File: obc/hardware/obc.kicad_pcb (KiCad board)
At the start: 4 copper layers, 80 x 80 mm, 61 parts, among them J1 Conn_ARM_JTAG_SWD_10, J2 Micro_SD_Card, J3 Conn_Coaxial, J4 USB_C_Receptacle_USB2.0_16P, J5 Conn_Coaxial, SW1 SW_SPDT, SW2 SW_Push, U1 STM32H743ZGT6, U2 RFM96W-433S2, U3 MAX6369, U4 MAX-M10S, U5 FM24CL16B, U6 MS5607-02BA, Y1 25 MHz, Y2 32.768 kHz

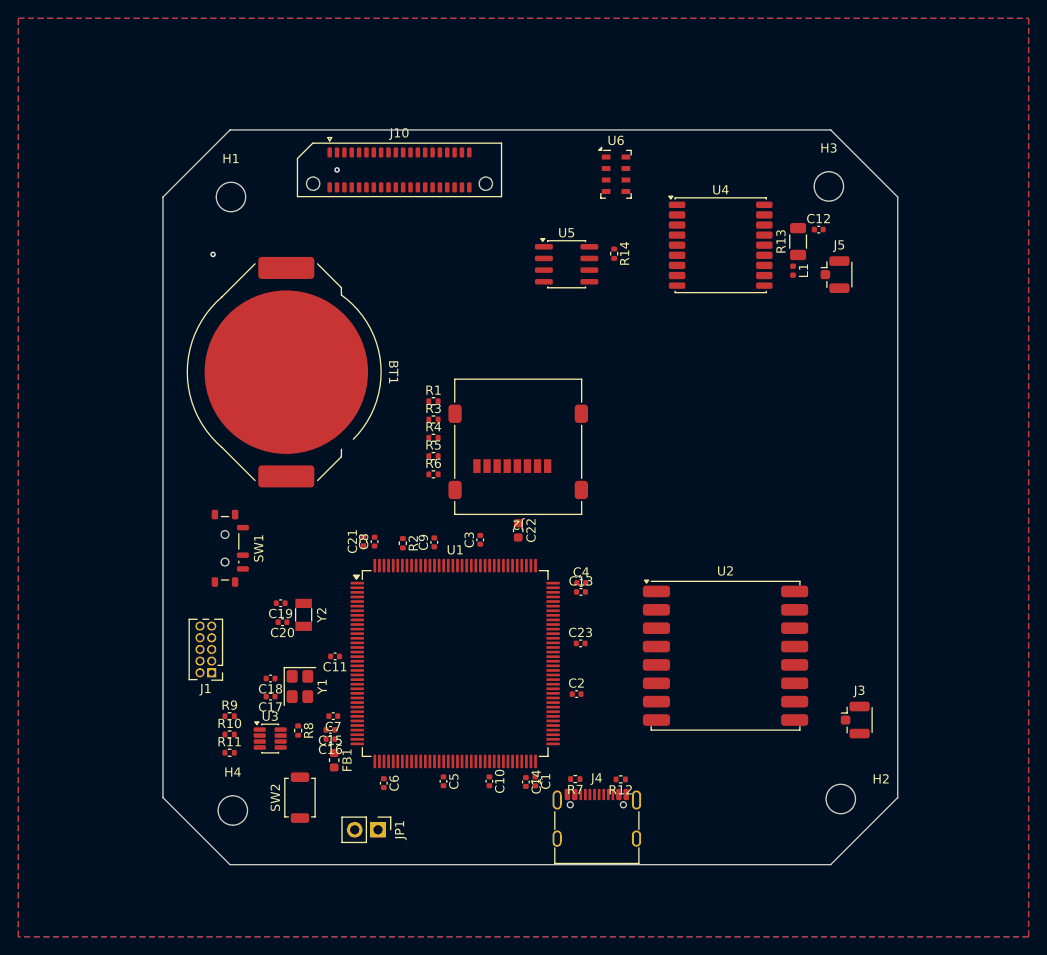
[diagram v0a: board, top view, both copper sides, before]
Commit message: added CAN, UART, supervisor, USB, power OR-ing, GPS, did layout
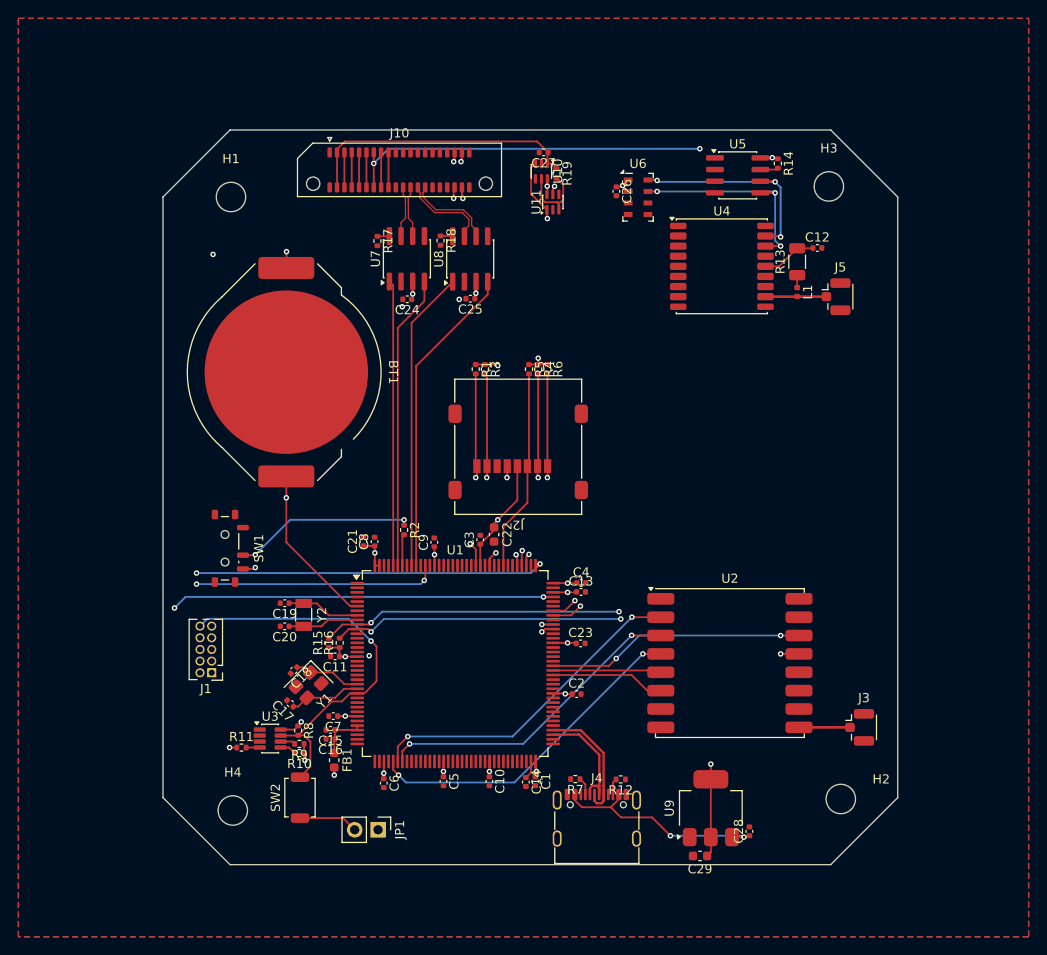
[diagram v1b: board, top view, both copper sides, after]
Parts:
- added C24: 100nF, Capacitor_SMD:C_0402_1005Metric, F.Cu at (117.3, 70.6)
- added C25: 100nF, Capacitor_SMD:C_0402_1005Metric, F.Cu at (124.2, 70.5)
- added C26: 100nF, Capacitor_SMD:C_0402_1005Metric, F.Cu at (140.1, 58.8)
- added C27: 10u, Capacitor_SMD:C_0402_1005Metric, F.Cu at (132.2, 54.6)
- added C28: 10u, Capacitor_SMD:C_0402_1005Metric, F.Cu at (154.6, 128.5)
- added C29: 22u, Capacitor_SMD:C_0603_1608Metric, F.Cu at (149.2, 131.2)
- added R15: 10k, Resistor_SMD:R_0402_1005Metric, F.Cu at (108.8, 108.0)
- added R16: 10k, Resistor_SMD:R_0402_1005Metric, F.Cu at (110.0, 108.0)
- added R17: 51k, Resistor_SMD:R_0402_1005Metric, F.Cu at (114.1, 64.2)
- added R18: 51k, Resistor_SMD:R_0402_1005Metric, F.Cu at (121.0, 64.2)
- added R19: 10k, Resistor_SMD:R_0402_1005Metric, F.Cu at (133.6, 56.9)
- added U10: LM66100DCK, Package_TO_SOT_SMD:SOT-363_SC-70-6, F.Cu at (131.9, 56.6)
- added U11: LM66100DCK, Package_TO_SOT_SMD:SOT-363_SC-70-6, F.Cu at (133.2, 60.0)
- added U7: SN65HVD230, Package_SO:SOIC-8_3.9x4.9mm_P1.27mm, F.Cu at (117.3, 66.2)
- added U8: SN65HVD230, Package_SO:SOIC-8_3.9x4.9mm_P1.27mm, F.Cu at (124.2, 66.2)
- added U9: AMS1117-3.3, Package_TO_SOT_SMD:SOT-223-3_TabPin2, F.Cu at (150.4, 126.0)
- moved U5 21.0 mm to (153.3, 57.1)
- moved R14 20.4 mm to (157.7, 55.8)
- moved R6 16.9 mm to (132.6, 78.2), turned to -90 degrees
- moved R5 14.1 mm to (130.6, 78.2), turned to -90 degrees
- moved R4 13.6 mm to (131.6, 78.2), turned to -90 degrees
- moved R9 8.17 mm to (105.6, 119.0), turned to 180 degrees
- moved R10 7.86 mm to (105.6, 120.0), turned to 180 degrees
- moved R3 7.84 mm to (125.8, 78.2), turned to -90 degrees
- moved R1 5.77 mm to (124.8, 78.2), turned to -90 degrees
- moved U6 3.47 mm to (142.5, 59.5)
- moved C18 2.69 mm to (105.0, 111.0), turned to -135 degrees
- moved C22 2.66 mm to (126.8, 96.2)
- moved J5 2.40 mm to (164.5, 70.3)
- moved L1 2.37 mm to (159.8, 69.8)
- moved U4 2.30 mm to (151.6, 67.0)
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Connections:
- net Net-(J5-In) renamed /STM32H7/Sensors/GPS_ANT
- C1 pad 1: +3.3V -> +3V3
- C10 pad 1: +3.3V -> +3V3
- C11 pad 1: +3.3V -> +3V3
- C2 pad 1: +3.3V -> +3V3
- C21 pad 1: +3.3V -> +3V3
- C22 pad 1: +3.3V -> +3V3
- C23 pad 1: +3.3V -> +3V3
- C3 pad 1: +3.3V -> +3V3
- C4 pad 1: +3.3V -> +3V3
- C5 pad 1: +3.3V -> +3V3
- C6 pad 1: +3.3V -> +3V3
- C7 pad 1: +3.3V -> +3V3
- C8 pad 1: +3.3V -> +3V3
- C9 pad 1: +3.3V -> +3V3
- FB1 pad 2: +3.3V -> +3V3
- J1 pad 1: +3.3V -> +3V3
- J10 pad 13: /Inter-Board-Connector/RAIL_6_VOUT -> VDD_RADIO
- J10 pad 14: /Inter-Board-Connector/RAIL_6_VOUT -> VDD_RADIO
- J10 pad 22: unconnected-(J10-Pin_22-Pad22) -> /Inter-Board-Connector/CAN_MAIN+
- J10 pad 24: unconnected-(J10-Pin_24-Pad24) -> /Inter-Board-Connector/CAN_MAIN-
- J10 pad 26: unconnected-(J10-Pin_26-Pad26) -> /Inter-Board-Connector/CAN_AUX+
- J10 pad 28: unconnected-(J10-Pin_28-Pad28) -> /Inter-Board-Connector/CAN_AUX-
- J10 pad 3: +3.3V -> /Inter-Board-Connector/RAIL_1_VOUT
- J10 pad 4: +3.3V -> /Inter-Board-Connector/RAIL_1_VOUT
- J2 pad 4: +3.3V -> +3V3
- R1 pad 1: +3.3V -> +3V3
- R10 pad 1: +3.3V -> +3V3
- R11 pad 1: +3.3V -> +3V3
- R14 pad 1: +3.3V -> +3V3
- R3 pad 1: +3.3V -> +3V3
- R4 pad 1: +3.3V -> +3V3
- R5 pad 1: +3.3V -> +3V3
- R6 pad 1: +3.3V -> +3V3
- R8 pad 1: +3.3V -> +3V3
- R9 pad 1: +3.3V -> +3V3
- SW1 pad 3: +3.3V -> +3V3
- U1 pad 10: unconnected-(U1-PF0-Pad10) -> SDA
- U1 pad 101: unconnected-(U1-PA9-Pad101) -> /Inter-Board-Connector/SYSTEM_MAIN_UART_TX
- U1 pad 102: unconnected-(U1-PA10-Pad102) -> /Inter-Board-Connector/SYSTEM_MAIN_UART_RX
- U1 pad 108: +3.3V -> +3V3
- U1 pad 11: unconnected-(U1-PF1-Pad11) -> SCL
- U1 pad 119: unconnected-(U1-PD5-Pad119) -> /Inter-Board-Connector/SYSTEM_AUX_UART_TX
- U1 pad 121: +3.3V -> +3V3
- U1 pad 122: unconnected-(U1-PD6-Pad122) -> /Inter-Board-Connector/SYSTEM_AUX_UART_RX
- U1 pad 131: +3.3V -> +3V3
- U1 pad 135: unconnected-(U1-PB5-Pad135) -> /STM32H7/CAN2_RX
- U1 pad 136: unconnected-(U1-PB6-Pad136) -> /STM32H7/CAN2_TX
- U1 pad 139: unconnected-(U1-PB8-Pad139) -> /STM32H7/CAN1_RX
- U1 pad 140: unconnected-(U1-PB9-Pad140) -> /STM32H7/CAN1_TX
- U1 pad 143: +3.3V -> +3V3
- U1 pad 144: +3.3V -> +3V3
- U1 pad 17: +3.3V -> +3V3
- U1 pad 30: +3.3V -> +3V3
- U1 pad 39: +3.3V -> +3V3
- U1 pad 41: unconnected-(U1-PA5-Pad41) -> /STM32H7/SPI1_SCK
- U1 pad 42: unconnected-(U1-PA6-Pad42) -> /STM32H7/SPI1_MISO
- U1 pad 43: unconnected-(U1-PA7-Pad43) -> /STM32H7/SPI1_MOSI
- U1 pad 52: +3.3V -> +3V3
- U1 pad 62: +3.3V -> +3V3
- U1 pad 72: +3.3V -> +3V3
- U1 pad 75: /STM32H7/USB_D- -> unconnected-(U1-PB14-Pad75)
- U1 pad 76: /STM32H7/USB_D+ -> unconnected-(U1-PB15-Pad76)
- U1 pad 84: +3.3V -> +3V3
- U1 pad 88: unconnected-(U1-PG3-Pad88) -> /STM32H7/~{RADIO_RESET}
- U1 pad 89: unconnected-(U1-PG4-Pad89) -> /STM32H7/~{RADIO_CS}
- U1 pad 90: unconnected-(U1-PG5-Pad90) -> /STM32H7/RADIO_DIO0
- U1 pad 95: +3.3V -> +3V3
- U2 pad 13: +3.3V -> VDD_RADIO
- U2 pad 14: unconnected-(U2-DIO0-Pad14) -> /STM32H7/RADIO_DIO0
- U2 pad 2: /STM32H7/Radio/MISO -> /STM32H7/SPI1_MISO
- U2 pad 3: /STM32H7/Radio/MOSI -> /STM32H7/SPI1_MOSI
- U2 pad 4: /STM32H7/Radio/SCK -> /STM32H7/SPI1_SCK
- U2 pad 5: /STM32H7/Radio/~{CS} -> /STM32H7/~{RADIO_CS}
- U2 pad 6: /STM32H7/Radio/~{RESET} -> /STM32H7/~{RADIO_RESET}
- U3 pad 8: +3.3V -> +3V3
- U5 pad 8: +3.3V -> +3V3
- U6 pad 1: unconnected-(U6-VDD-Pad1) -> +3V3
- U6 pad 2: unconnected-(U6-PS-Pad2) -> +3V3
- U6 pad 3: unconnected-(U6-GND-Pad3) -> GND
- U6 pad 4: Net-(U6-CSB-Pad4) -> GND
- U6 pad 5: Net-(U6-CSB-Pad4) -> GND
- U6 pad 7: unconnected-(U6-SDI/SDA-Pad7) -> SDA
- U6 pad 8: unconnected-(U6-SCLK-Pad8) -> SCL
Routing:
- net SCL: track 0.00 -> 105.1 mm, vias 0 -> 5
- net SDA: track 0.00 -> 103.5 mm, vias 0 -> 5
- net VDD_RADIO: track 0.00 -> 100.6 mm, vias 0 -> 3
- net Net-(U10-~{CE}): track 0.00 -> 83.9 mm, vias 0 -> 2
- net +3V3: track 0.00 -> 62.2 mm, vias 0 -> 24
- net /Inter-Board-Connector/SYSTEM_MAIN_UART_TX: track 0.00 -> 58.2 mm, vias 0 -> 2
- net /Inter-Board-Connector/SYSTEM_MAIN_UART_RX: track 0.00 -> 57.1 mm, vias 0 -> 2
- net /STM32H7/SWDIO: track 0.00 -> 49.9 mm, vias 0 -> 2
- net /STM32H7/SWCLK: track 0.00 -> 49.3 mm, vias 0 -> 2
- net Net-(BT1-+): track 0.00 -> 46.6 mm, vias 0 -> 2
- net /Inter-Board-Connector/SYSTEM_AUX_UART_RX: track 0.00 -> 43.9 mm, vias 0 -> 2
- net /STM32H7/NRST: track 0.00 -> 43.4 mm, vias 0 -> 1
- net /Inter-Board-Connector/SYSTEM_AUX_UART_TX: track 0.00 -> 43.0 mm, vias 0 -> 2
- net /STM32H7/SPI1_SCK: track 0.00 -> 36.4 mm, vias 0 -> 2
- net /STM32H7/SPI1_MISO: track 0.00 -> 36.1 mm, vias 0 -> 2
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- added copper zone on In2.Cu, net +3V3
- removed copper zone on In2.Cu, net +3.3V

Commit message: Redid silkscreen
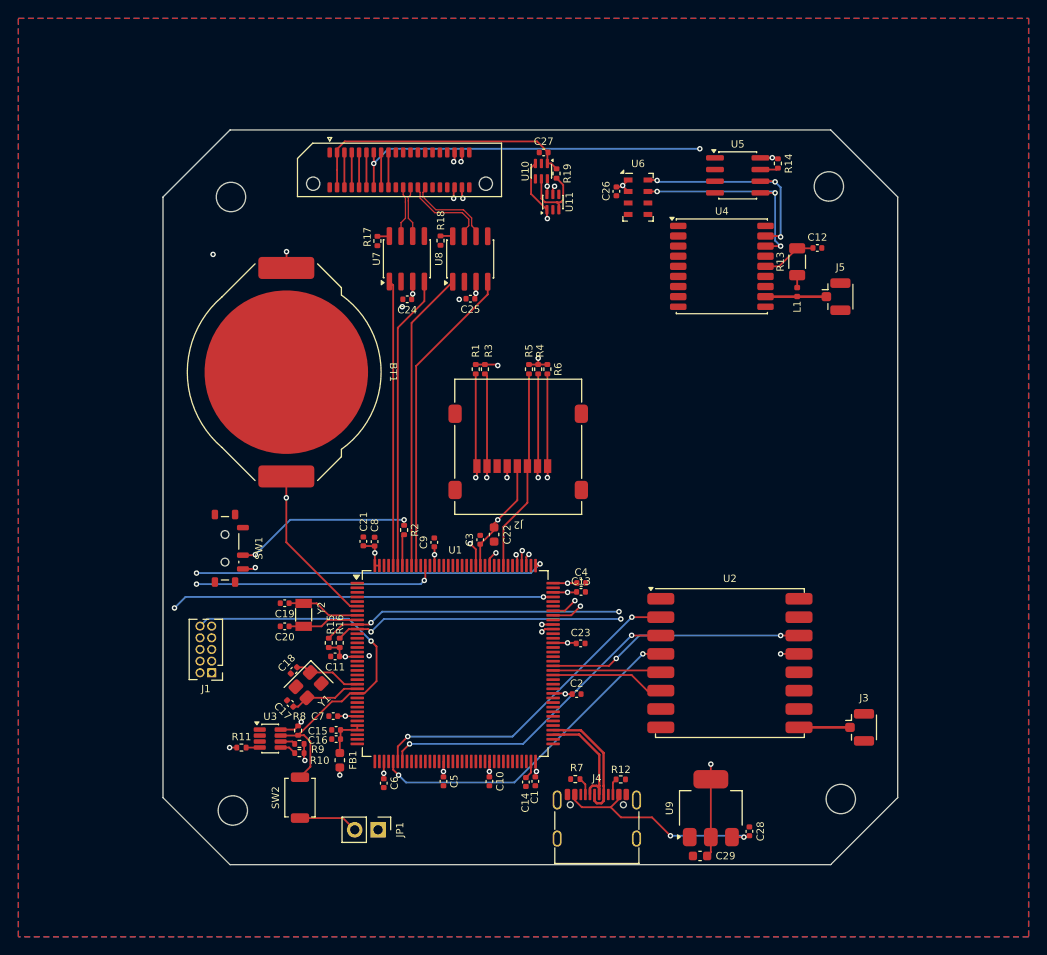
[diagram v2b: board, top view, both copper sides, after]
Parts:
- added REF**: Smolhaj_Scale_0.1, Symbol:Smolhaj_Scale_0.1, B.Cu at (100.6, 69.2)
- added REF**: Smolhaj_Scale_0.1, Symbol:Smolhaj_Scale_0.1, B.Cu at (101.4, 92.2)
- added REF**: Smolhaj_Scale_0.1, Symbol:Smolhaj_Scale_0.1, B.Cu at (101.8, 115.2)
- moved C15 0.61 mm to (109.6, 117.5)
- moved C16 0.61 mm to (109.6, 118.5)
- moved FB1 0.61 mm to (110.0, 120.8)
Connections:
- U1 pad 75: unconnected-(U1-PB14-Pad75) -> /STM32H7/USB_D-
- U1 pad 76: unconnected-(U1-PB15-Pad76) -> /STM32H7/USB_D+
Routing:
- net VDDA: track 5.49 -> 4.88 mm

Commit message: add SCRT and OSU AIAA logos, add IMU, add PPS LED, hook up some IOs
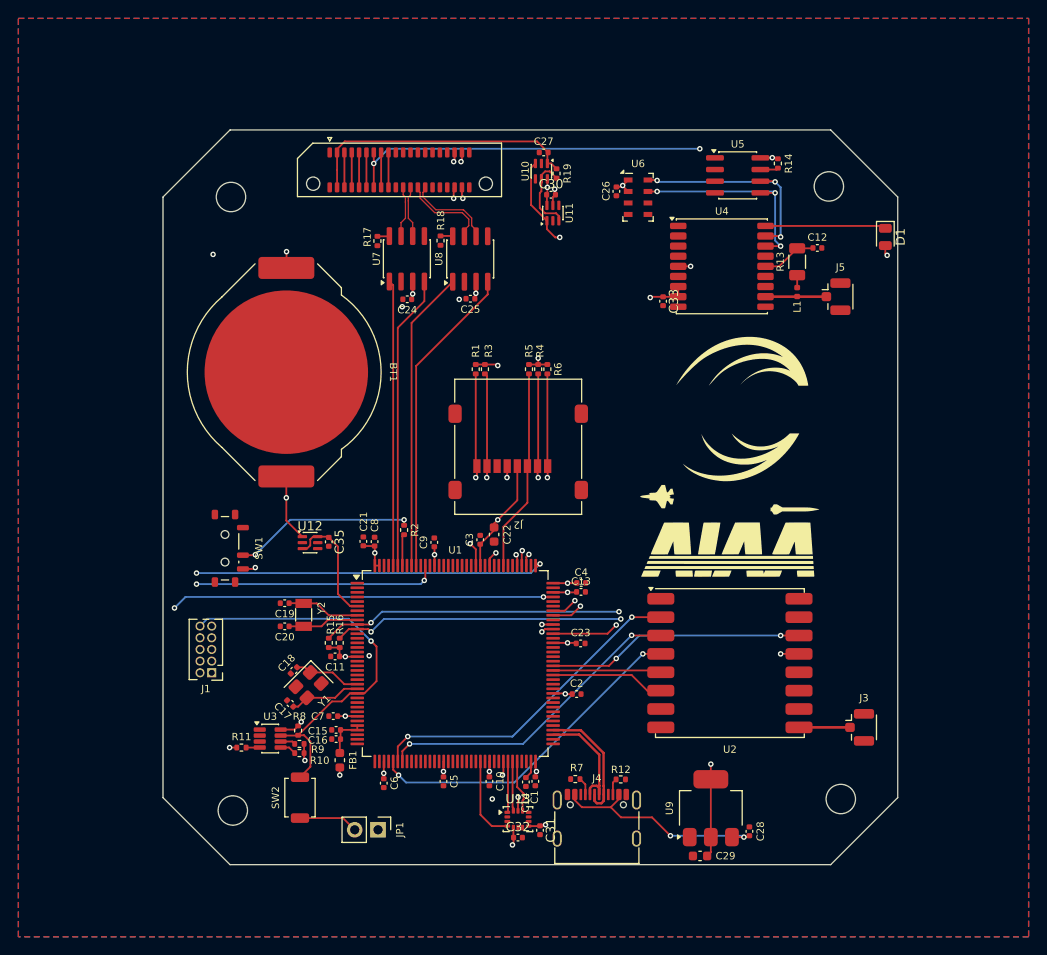
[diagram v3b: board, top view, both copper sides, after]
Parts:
- removed the REF** at (100.6, 69.2)
- removed the REF** at (101.8, 115.2)
- added C30: 10u, Capacitor_SMD:C_0402_1005Metric, F.Cu at (133.0, 59.2)
- added C31: 100nF, Capacitor_SMD:C_0402_1005Metric, F.Cu at (131.8, 128.4)
- added C32: 100nF, Capacitor_SMD:C_0402_1005Metric, F.Cu at (129.4, 129.2)
- added C33: 100nF, Capacitor_SMD:C_0402_1005Metric, F.Cu at (145.2, 70.8)
- added C35: 100nF, Capacitor_SMD:C_0402_1005Metric, F.Cu at (108.8, 97.0)
- added D1: LED, LED_SMD:LED_0805_2012Metric, F.Cu at (169.4, 63.8)
- added REF**: osu-aiaa-logo, obc-footprints:osu-aiaa-logo, F.Cu at (142.8, 100.8)
- added REF**: scrt-logo, obc-footprints:scrt-logo, F.Cu at (153.6, 82.6)
- added U12: LM66100DCK, Package_TO_SOT_SMD:SOT-363_SC-70-6, F.Cu at (106.8, 97.1)
- added U13: LSM6DSM, Package_LGA:LGA-14_3x2.5mm_P0.5mm_LayoutBorder3x4y, F.Cu at (129.4, 127.2)
- moved U11 1.20 mm to (133.2, 61.2)
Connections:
- U1 pad 6: Net-(BT1-+) -> Net-(U1-VBAT)
- U1 pad 60: unconnected-(U1-PE9-Pad60) -> /STM32H7/Sensors/IMU_INTERRUPT
- U1 pad 65: unconnected-(U1-PE12-Pad65) -> /STM32H7/SPI4_SCK
- U1 pad 66: unconnected-(U1-PE13-Pad66) -> /STM32H7/SPI4_MISO
- U1 pad 67: unconnected-(U1-PE14-Pad67) -> /STM32H7/SPI4_MOSI
- U1 pad 68: unconnected-(U1-PE15-Pad68) -> /STM32H7/Sensors/~{IMU_CS}
- U1 pad 97: unconnected-(U1-PC7-Pad97) -> /STM32H7/GPS_EXTINT
- U4 pad 18: unconnected-(U4-~{SAFEBOOT}-Pad18) -> Net-(D1-K)
- U4 pad 5: /STM32H7/Sensors/GPS_EXTINT -> /STM32H7/GPS_EXTINT
- U4 pad 7: unconnected-(U4-VCC_IO-Pad7) -> +3V3
- U4 pad 8: unconnected-(U4-VCC-Pad8) -> +3V3
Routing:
- net /STM32H7/GPS_EXTINT: track 0.00 -> 52.1 mm, vias 0 -> 2
- net Net-(D1-K): track 0.00 -> 13.2 mm
- net Net-(U1-VBAT): track 0.00 -> 13.0 mm
- net +3V3: track 62.2 -> 72.7 mm, vias 24 -> 28
- net Net-(BT1-+): track 46.6 -> 36.3 mm
- net /STM32H7/Sensors/IMU_INTERRUPT: track 0.00 -> 9.24 mm
- net /STM32H7/SPI4_SCK: track 0.00 -> 6.13 mm, vias 0 -> 2
- net /STM32H7/Sensors/~{IMU_CS}: track 0.00 -> 5.71 mm
- net /STM32H7/SPI4_MISO: track 0.00 -> 5.57 mm
- net /STM32H7/SPI4_MOSI: track 0.00 -> 5.41 mm
- net GND: track 0.95 -> 1.91 mm, vias 5 -> 6
